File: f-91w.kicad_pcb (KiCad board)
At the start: 4 copper layers, 24.4 x 24.4 mm, 37 parts, among them P10 CONN_01X01, P11 CONN_01X01, P13 CONN_01X01, P14 CONN_01X01, P5 CONN_01X01, P6 CONN_01X01, P7 CONN_01X01, P8 CONN_01X01, P9 CONN_01X01, Q1 BC846, U1 CY8C4248LQI-BL483, U2 LCD-F-91W, U3 BME680, Y1 32.768KHz, Y2 24MHz

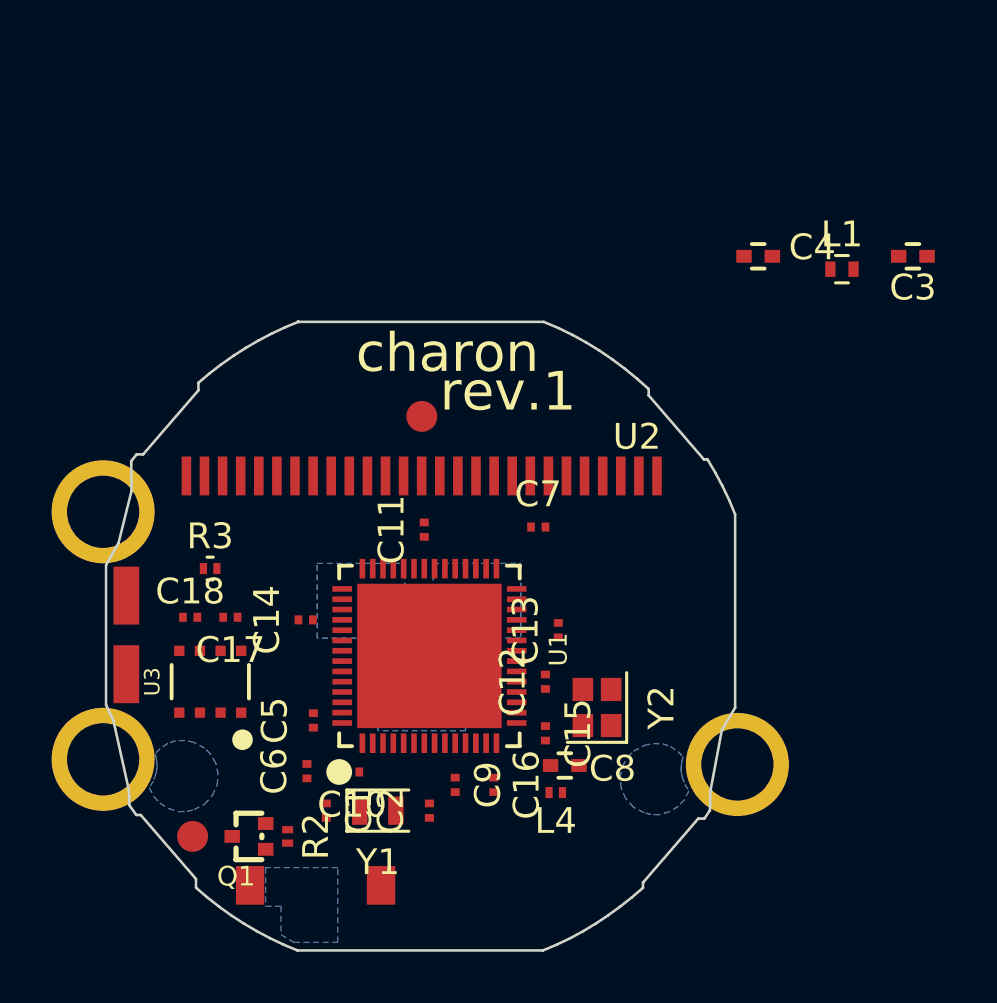
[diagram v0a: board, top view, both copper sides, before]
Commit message: Put in design rules for PCBCart, tidy up placement
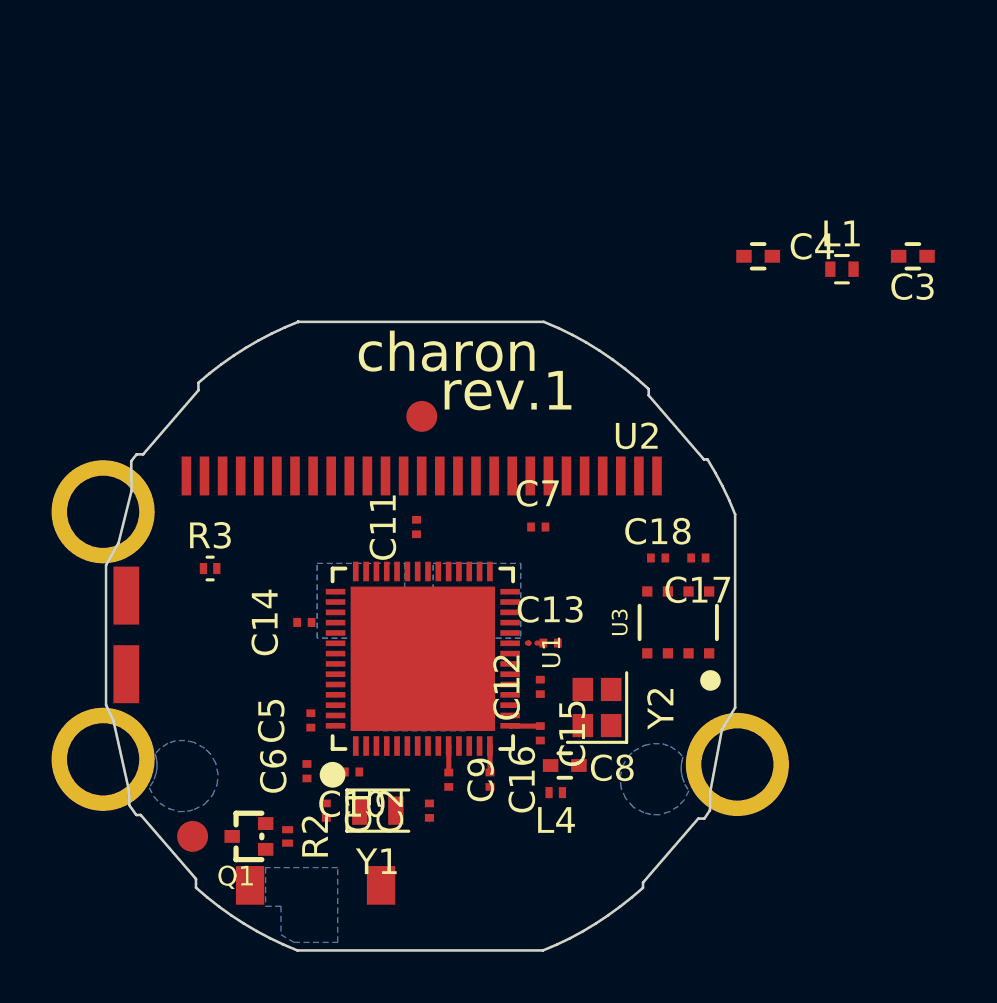
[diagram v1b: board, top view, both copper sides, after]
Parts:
- moved C17 18.3 mm to (68.7, 94.1)
- moved C18 18.3 mm to (67.1, 94.1)
- moved U3 18.3 mm to (67.9, 96.6)
- moved C13 0.58 mm to (63.0, 97.4), turned to 0 degrees
- moved C9 0.32 mm to (59.0, 102.7)
- moved C11 0.32 mm to (57.8, 92.9)
- moved C12 0.28 mm to (62.6, 99.1)
- moved U1 0.28 mm to (58.0, 98.0)
- moved C16 0.25 mm to (60.6, 102.7)
- moved C15 0.20 mm to (62.6, 100.9)
- moved C14 0.11 mm to (53.4, 96.6)
- moved C5 0.10 mm to (53.7, 100.4)
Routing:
- net VDDR: track 0.00 -> 3.23 mm
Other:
- net class Default: trace_width 0.2 -> 0.15; via_dia 0.46 -> 0.35; via_drill 0.3 -> 0.2
- net class PWR: trace_width 0.3 -> 0.2; via_dia 0.6 -> 0.35; via_drill 0.4 -> 0.2
- rule trace_min: 0.1524 -> 0.127
- rule via_min_drill: 0.3 -> 0.2
- rule via_min_size: 0.46 -> 0.35
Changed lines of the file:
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@@
     (thickness 0.6)
     (drawings 507)
-    (tracks 0)
+    (tracks 10)
     (zones 0)
     (modules 37)
@@
     (1 In1.Cu signal)
     (2 In2.Cu signal)
-    (31 B.Cu signal)
+    (31 B.Cu signal hide)
     (32 B.Adhes user)
     (33 F.Adhes user)
-    (34 B.Paste user)
+    (34 B.Paste user hide)
     (35 F.Paste user)
-    (36 B.SilkS user)
-    (37 F.SilkS user)
+    (36 B.SilkS user hide)
+    (37 F.SilkS user hide)
     (38 B.Mask user)
     (39 F.Mask user)
-    (40 Dwgs.User user)
+    (40 Dwgs.User user hide)
     (41 Cmts.User user)
     (42 Eco1.User user)
@@
     (44 Edge.Cuts user)
     (45 Margin user)
-    (46 B.CrtYd user)
-    (47 F.CrtYd user)
-    (48 B.Fab user)
-    (49 F.Fab user)
+    (46 B.CrtYd user hide)
+    (47 F.CrtYd user hide)
+    (48 B.Fab user hide)
+    (49 F.Fab user hide)
   )
   (setup
-    (last_trace_width 0.2)
+    (last_trace_width 0.3)
     (user_trace_width 0.2)
     (user_trace_width 0.3)
@@
     (zone_clearance 0.2)
     (zone_45_only no)
-    (trace_min 0.1524)
+    (trace_min 0.127)
     (segment_width 0.2)
     (edge_width 0.2)
-    (via_size 0.46)
-    (via_drill 0.3)
-    (via_min_size 0.46)
-    (via_min_drill 0.3)
+    (via_size 0.35)
+    (via_drill 0.2)
+    (via_min_size 0.35)
+    (via_min_drill 0.2)
     (uvia_size 0.3)
     (uvia_drill 0.1)
@@
     (mod_text_size 1 1)
     (mod_text_width 0.15)
-    (pad_size 0.8 0.3)
+    (pad_size 5.6 5.6)
     (pad_drill 0)
     (pad_to_mask_clearance 0.1)
@@
   (net_class Default "This is the default net class."
     (clearance 0.1524)
-    (trace_width 0.2)
-    (via_dia 0.46)
-    (via_drill 0.3)
+    (trace_width 0.15)
+    (via_dia 0.35)
+    (via_drill 0.2)
     (uvia_dia 0.3)
     (uvia_drill 0.1)
@@
   (net_class PWR ""
     (clearance 0.1524)
-    (trace_width 0.3)
-    (via_dia 0.6)
-    (via_drill 0.4)
+    (trace_width 0.2)
+    (via_dia 0.35)
+    (via_drill 0.2)
     (uvia_dia 0.3)
     (uvia_drill 0.1)
@@
   )
   (module Capacitors_SMD:C_0201_NoSilk (layer F.Cu)
-    (at 53.7555 100.391 270)
+    (at 53.6555 100.391 270)
     (descr "Capacitor SMD 0201, reflow soldering, AVX (see smccp.pdf)")
     (tags "capacitor 0201")
@@
   )
   (module Capacitors_SMD:C_0201_NoSilk (layer F.Cu)
-    (at 59.2555 102.891 270)
+    (at 59.0055 102.691 270)
     (descr "Capacitor SMD 0201, reflow soldering, AVX (see smccp.pdf)")
     (tags "capacitor 0201")
@@
   )
   (module Capacitors_SMD:C_0201_NoSilk (layer F.Cu)
-    (at 58.0555 92.991 90)
+    (at 57.7555 92.891 90)
     (descr "Capacitor SMD 0201, reflow soldering, AVX (see smccp.pdf)")
     (tags "capacitor 0201")
@@
   )
   (module Capacitors_SMD:C_0201_NoSilk (layer F.Cu)
-    (at 62.7555 98.891 90)
+    (at 62.5555 99.091 90)
     (descr "Capacitor SMD 0201, reflow soldering, AVX (see smccp.pdf)")
     (tags "capacitor 0201")
@@
   )
   (module Capacitors_SMD:C_0201_NoSilk (layer F.Cu)
-    (at 63.2555 96.891 90)
+    (at 62.9555 97.391)
     (descr "Capacitor SMD 0201, reflow soldering, AVX (see smccp.pdf)")
     (tags "capacitor 0201")
     (attr smd)
-    (fp_text reference C13 (at 0 -1.27 90) (layer F.SilkS)
-      (effects (font (size 1 1) (thickness 0.15)))
-    )
-    (fp_text value 100nF (at 0 1.27 90) (layer F.Fab)
-      (effects (font (size 1 1) (thickness 0.15)))
-    )
-    (fp_text user %R (at 0 -1.27 90) (layer F.Fab)
+    (fp_text reference C13 (at 0 -1.27) (layer F.SilkS)
+      (effects (font (size 1 1) (thickness 0.15)))
+    )
+    (fp_text value 100nF (at 0 1.27) (layer F.Fab)
+      (effects (font (size 1 1) (thickness 0.15)))
+    )
+    (fp_text user %R (at 0 -1.27) (layer F.Fab)
       (effects (font (size 1 1) (thickness 0.15)))
     )
@@
     (fp_line (start 0.58 0.32) (end 0.58 -0.33) (layer F.CrtYd) (width 0.05))
     (fp_line (start 0.58 0.32) (end -0.58 0.32) (layer F.CrtYd) (width 0.05))
-    (pad 1 smd rect (at -0.28 0 90) (size 0.3 0.35) (layers F.Cu F.Paste F.Mask)
+    (pad 1 smd rect (at -0.28 0) (size 0.3 0.35) (layers F.Cu F.Paste F.Mask)
       (net 6 VCC))
-    (pad 2 smd rect (at 0.28 0 90) (size 0.3 0.35) (layers F.Cu F.Paste F.Mask)
+    (pad 2 smd rect (at 0.28 0) (size 0.3 0.35) (layers F.Cu F.Paste F.Mask)
       (net 2 GND))
     (model Capacitors_SMD.3dshapes/C_0201.wrl
@@
   )
   (module Capacitors_SMD:C_0201_NoSilk (layer F.Cu)
-    (at 53.4555 96.491 180)
+    (at 53.4055 96.591 180)
     (descr "Capacitor SMD 0201, reflow soldering, AVX (see smccp.pdf)")
     (tags "capacitor 0201")
@@
   )
   (module Capacitors_SMD:C_0201_NoSilk (layer F.Cu)
-    (at 62.7555 100.891 270)
+    (at 62.5555 100.891 270)
     (descr "Capacitor SMD 0201, reflow soldering, AVX (see smccp.pdf)")
     (tags "capacitor 0201")
@@
   )
   (module Capacitors_SMD:C_0201_NoSilk (layer F.Cu)
-    (at 60.7555 102.891 270)
+    (at 60.6055 102.691 270)
     (descr "Capacitor SMD 0201, reflow soldering, AVX (see smccp.pdf)")
     (tags "capacitor 0201")
@@
   )
   (module Capacitors_SMD:C_0201_NoSilk (layer F.Cu)
-    (at 50.5355 96.391 180)
+    (at 68.6855 94.091 180)
     (descr "Capacitor SMD 0201, reflow soldering, AVX (see smccp.pdf)")
     (tags "capacitor 0201")
@@
   )
   (module Capacitors_SMD:C_0201_NoSilk (layer F.Cu)
-    (at 48.9755 96.391 180)
+    (at 67.1255 94.091 180)
     (descr "Capacitor SMD 0201, reflow soldering, AVX (see smccp.pdf)")
     (tags "capacitor 0201")
@@
   )
   (module f-91w:Cypress_QFN56 (layer F.Cu)
-    (at 58.2555 97.891 90)
+    (at 58 98 90)
     (fp_text reference U1 (at 0.25 5 90) (layer F.SilkS)
       (effects (font (size 0.7 0.7) (thickness 0.15)))
@@
   )
   (module f-91w:BME680 (layer F.Cu)
-    (at 49.7555 98.891 270)
+    (at 67.9055 96.591 270)
     (fp_text reference U3 (at 0 2.25 270) (layer F.SilkS)
       (effects (font (size 0.6 0.6) (thickness 0.15)))
@@
   (gr_line (start 55.529166 85.5) (end 55 86.029167) (layer Dwgs.User) (width 0.1))
   (gr_line (start 55 85.5) (end 55.529166 86.029167) (layer Dwgs.User) (width 0.1))
+  (segment (start 62.6755 97.391) (end 62.4255 97.391) (width 0.2) (layer F.Cu) (net 6))
+  (segment (start 62.0555 97.391) (end 62.112584 97.391) (width 0.2) (layer F.Cu) (net 6))
+  (segment (start 62.112584 97.391) (end 62.116451 97.394867) (width 0.2) (layer F.Cu) (net 6))
+  (segment (start 61.394 97.391) (end 61.385 97.4) (width 0.2) (layer F.Cu) (net 6))
+  (segment (start 62.5555 100.611) (end 61.396 100.611) (width 0.2) (layer F.Cu) (net 11))
+  (segment (start 61.396 100.611) (end 61.385 100.6) (width 0.2) (layer F.Cu) (net 11))
+  (segment (start 60.6055 102.411) (end 60.6055 101.3905) (width 0.2) (layer F.Cu) (net 11))
+  (segment (start 60.6055 101.3905) (end 60.6 101.385) (width 0.2) (layer F.Cu) (net 11))
+  (segment (start 59.0055 102.411) (end 59.0055 101.3905) (width 0.2) (layer F.Cu) (net 11))
+  (segment (start 59.0055 101.3905) (end 59 101.385) (width 0.2) (layer F.Cu) (net 11))
   (zone (net 2) (net_name GND) (layer B.Cu) (hatch edge 0.508)
     (connect_pads (clearance 0.2))

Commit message: PCB: Route LCD display
Some space left for debug test points, TBD
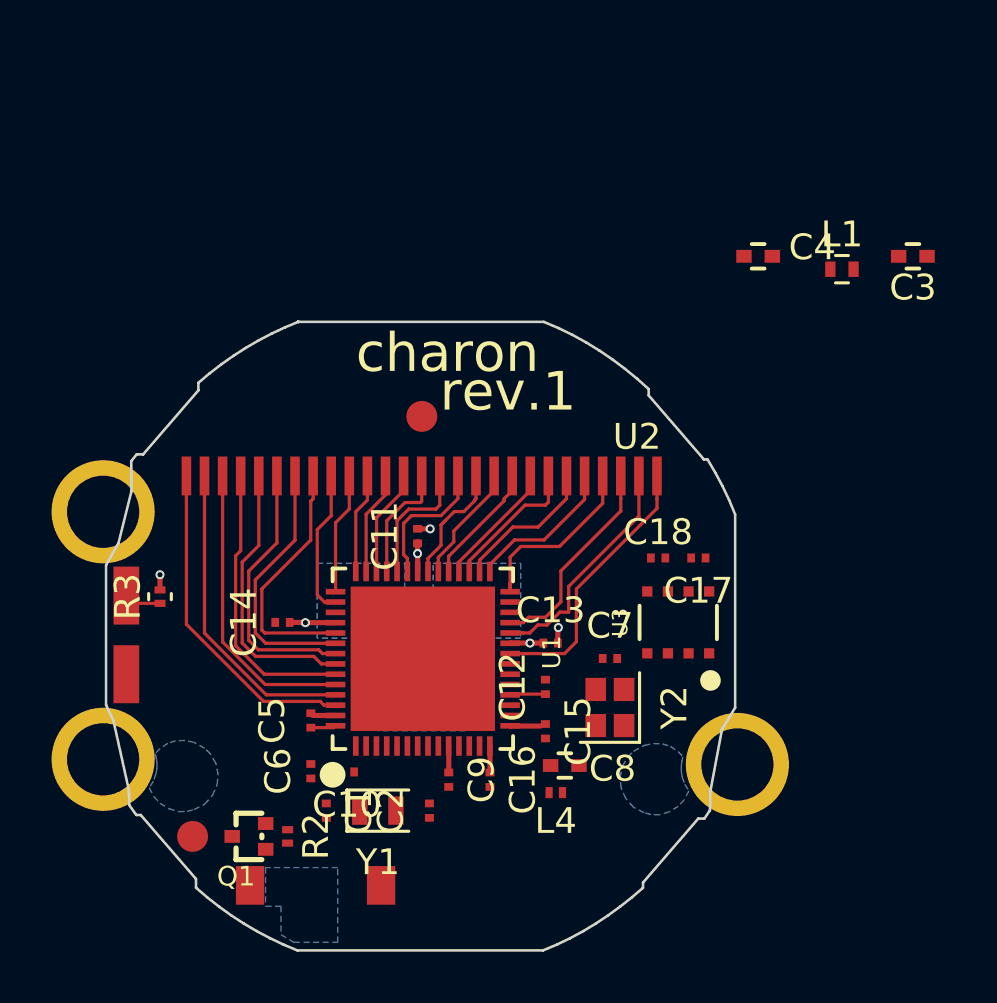
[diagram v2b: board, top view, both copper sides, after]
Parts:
- moved C7 5.81 mm to (65.3, 98.0)
- moved R3 2.23 mm to (47.8, 95.6), turned to 90 degrees
- moved C14 0.85 mm to (52.6, 96.6)
- moved Y2 0.50 mm to (65.3, 99.9)
- moved C11 0.35 mm to (57.8, 93.2)
- moved C15 0.22 mm to (62.8, 100.8)
- moved C10 0.20 mm to (55.1, 102.4)
- moved C12 0.20 mm to (62.8, 99.1)
- moved C6 0.15 mm to (53.7, 102.4)
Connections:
- P11 pad 1: (no net) -> /LED_1
- P5 pad 1: (no net) -> /B_LIGHT
- P6 pad 1: (no net) -> /B_MODE
- P7 pad 1: (no net) -> /B_ALARM
- R2 pad 1: (no net) -> /BUZ_EN
- R3 pad 2: (no net) -> VCC
- U1 pad 18: (no net) -> VDDR
- U1 pad 19: (no net) -> /SDA
- U1 pad 20: (no net) -> /SCL
- U1 pad 21: (no net) -> /B_ALARM
- U1 pad 22: (no net) -> /LCD_SEG24
- U1 pad 24: (no net) -> /LCD_SEG23
- U1 pad 25: (no net) -> /LCD_SEG22
- U1 pad 28: (no net) -> /LCD_SEG21
- U1 pad 29: (no net) -> /LCD_SEG20
- U1 pad 30: (no net) -> /LCD_SEG19
- U1 pad 31: (no net) -> /LCD_SEG18
- U1 pad 32: (no net) -> /LCD_SEG17
- U1 pad 33: (no net) -> /LCD_SEG16
- U1 pad 34: (no net) -> /LCD_SEG15
- U1 pad 35: (no net) -> /LCD_SEG14
- U1 pad 37: (no net) -> /LCD_SEG13
- U1 pad 38: (no net) -> /LCD_SEG12
- U1 pad 39: (no net) -> /LCD_SEG11
- U1 pad 40: (no net) -> /LCD_SEG10
- U1 pad 41: (no net) -> /LCD_SEG9
- U1 pad 42: (no net) -> /LCD_SEG8
- U1 pad 43: (no net) -> /LCD_SEG7
- U1 pad 44: (no net) -> /LCD_COM3
- U1 pad 47: (no net) -> /LCD_COM2
- U1 pad 48: (no net) -> /LCD_COM1
- U1 pad 49: (no net) -> /LCD_SEG6
- U1 pad 5: (no net) -> /B_LIGHT
- U1 pad 50: (no net) -> /LCD_SEG5
- U1 pad 51: (no net) -> /LCD_SEG4
- U1 pad 52: (no net) -> /LCD_SEG3
- U1 pad 53: (no net) -> /LCD_SEG2
- U1 pad 54: (no net) -> /LCD_SEG1
- U1 pad 6: (no net) -> /LED_1
- U1 pad 7: (no net) -> /B_MODE
- U1 pad 8: (no net) -> /BUZ_EN
- U2 pad 1: (no net) -> /LCD_SEG1
- U2 pad 10: (no net) -> /LCD_SEG7
- U2 pad 11: (no net) -> /LCD_SEG8
- U2 pad 12: (no net) -> /LCD_SEG9
- U2 pad 13: (no net) -> /LCD_SEG10
- U2 pad 14: (no net) -> /LCD_SEG11
- U2 pad 15: (no net) -> /LCD_SEG12
- U2 pad 16: (no net) -> /LCD_SEG13
- U2 pad 17: (no net) -> /LCD_SEG14
- U2 pad 18: (no net) -> /LCD_SEG15
- U2 pad 19: (no net) -> /LCD_SEG16
- U2 pad 2: (no net) -> /LCD_SEG2
- U2 pad 20: (no net) -> /LCD_SEG17
- U2 pad 21: (no net) -> /LCD_SEG18
- U2 pad 22: (no net) -> /LCD_SEG19
- U2 pad 23: (no net) -> /LCD_SEG20
- U2 pad 24: (no net) -> /LCD_SEG21
- U2 pad 25: (no net) -> /LCD_SEG22
- U2 pad 26: (no net) -> /LCD_SEG23
- U2 pad 27: (no net) -> /LCD_SEG24
- U2 pad 3: (no net) -> /LCD_SEG3
- U2 pad 4: (no net) -> /LCD_SEG4
- U2 pad 5: (no net) -> /LCD_SEG5
- U2 pad 6: (no net) -> /LCD_SEG6
- U2 pad 7: (no net) -> /LCD_COM1
- U2 pad 8: (no net) -> /LCD_COM2
- U2 pad 9: (no net) -> /LCD_COM3
- U3 pad 3: (no net) -> /SDA
- U3 pad 4: (no net) -> /SCL
- Y2 pad 2: (no net) -> GND
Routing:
- net /LCD_SEG1: track 0.00 -> 12.8 mm
- net /LCD_SEG2: track 0.00 -> 12.2 mm
- net /LCD_SEG3: track 0.00 -> 11.5 mm
- net /LCD_SEG4: track 0.00 -> 11.0 mm
- net /LCD_SEG5: track 0.00 -> 10.7 mm
- net /LCD_SEG24: track 0.00 -> 10.5 mm
- net /LCD_SEG6: track 0.00 -> 10.4 mm
- net /LCD_COM1: track 0.00 -> 10.0 mm
- net /LCD_COM2: track 0.00 -> 9.71 mm
- net /LCD_SEG23: track 0.00 -> 9.04 mm
- net /LCD_SEG22: track 0.00 -> 8.15 mm
- net /LCD_SEG21: track 0.00 -> 7.76 mm
- net /LCD_SEG20: track 0.00 -> 6.47 mm
- net /LCD_SEG19: track 0.00 -> 5.68 mm
- net /LCD_COM3: track 0.00 -> 5.66 mm
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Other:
- net class Default: clearance 0.1524 -> 0.127; trace_width 0.15 -> 0.127
- net class PWR: clearance 0.1524 -> 0.127
- rule trace_clearance: 0.1524 -> 0.127
- rule via_min_size: 0.35 -> 0.2

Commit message: More routing, add planes, crystals and decoupling caps
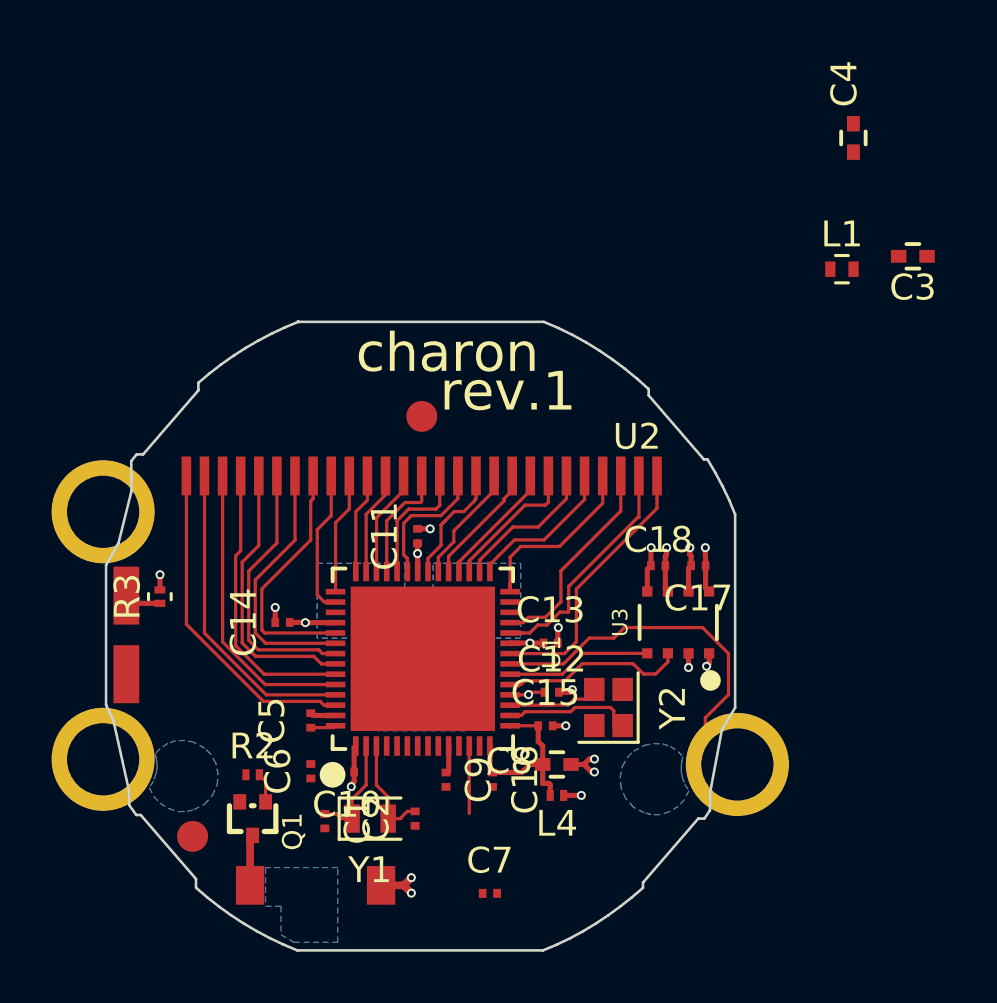
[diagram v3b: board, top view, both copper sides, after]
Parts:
- moved C7 10.2 mm to (60.6, 107.1)
- moved C4 5.89 mm to (74.7, 77.8), turned to 270 degrees
- moved R2 2.75 mm to (51.4, 102.5), turned to 0 degrees
- moved Q1 0.71 mm to (51.4, 104.2), turned to 270 degrees
- moved C2 0.64 mm to (57.7, 104.2)
- moved Y1 0.43 mm to (56.0, 104.2)
- moved C1 0.41 mm to (54.2, 104.3)
- moved C12 0.32 mm to (63.0, 99.3), turned to 0 degrees
- moved C8 0.31 mm to (63.2, 102.1), turned to 0 degrees
- moved C17 0.30 mm to (68.7, 94.4)
- moved C18 0.30 mm to (67.1, 94.4)
- moved C15 0.21 mm to (62.8, 100.6), turned to 0 degrees
- moved L4 0.12 mm to (63.2, 103.3)
- moved C9 0.11 mm to (58.9, 102.7)
- moved C16 0.09 mm to (60.7, 102.7)
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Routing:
- net /B_ALARM: track 0.00 -> 14.7 mm
- net VCC: track 4.89 -> 13.0 mm, vias 4 -> 11
- net GND: track 2.09 -> 9.33 mm, vias 2 -> 10
- net /SDA: track 0.00 -> 7.14 mm
- net /SCL: track 0.00 -> 5.66 mm
- net VDDR: track 4.41 -> 9.69 mm, vias 0 -> 1
- net Net-(U1-Pad16): track 0.00 -> 4.78 mm
- net Net-(C1-Pad1): track 0.00 -> 4.18 mm
- net Net-(C2-Pad1): track 0.00 -> 4.18 mm
- net Net-(U1-Pad17): track 0.00 -> 3.52 mm
- net Net-(C4-Pad1): track 0.00 -> 2.61 mm
- net /BUZ: track 0.00 -> 2.05 mm
- net Net-(Q1-Pad1): track 0.00 -> 1.15 mm
- added copper zone on In1.Cu, net GND
- added copper zone on In2.Cu, net VCC
